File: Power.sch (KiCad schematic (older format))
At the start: 0 parts

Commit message: Put the power schematic in the wrong sub-module (PowerAdjustmentMonitor)
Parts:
- added C? (x2): C, ~, symbol C
- added F? (x4): FUSE, ~, symbol FUSE
- added L? (x2): INDUCTOR, ~, symbol INDUCTOR
- added P?: CONN_12X2, symbol CONN_12X2
- added R?: R, ~, symbol R
- added SW?: SWITCH_INV, ~, symbol SWITCH_INV
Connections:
- net labels added: +12P, +12V, +3.3V, +5V, -12P, -12V, GND
- wire segments 0 -> 36

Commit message: 3.10   Revisiting The Current/Fan Module End of Module 3, lots of cleanup/changes all over the place.
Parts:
- removed F? (x4): FUSE, ~, symbol FUSE
- added TH? (x4): THERMISTOR, ~, symbol THERMISTOR
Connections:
- net labels added: +12C
- wire segments 36 -> 33
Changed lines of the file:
@@
 $Descr A4 11693 8268
 encoding utf-8
-Sheet 4 9
+Sheet 3 9
 Title ""
 Date "10 feb 2014"
@@
 $EndComp
 $Comp
-L FUSE F?
-U 1 1 52F47ADD
-P 3800 2100
-F 0 "F?" H 3900 2150 40  0000 C CNN
-F 1 "FUSE" H 3700 2050 40  0000 C CNN
-F 2 "~" H 3800 2100 60  0000 C CNN
-F 3 "~" H 3800 2100 60  0000 C CNN
-	1    3800 2100
-	1    0    0    -1
-$EndComp
-$Comp
-L FUSE F?
-U 1 1 52F47AE3
-P 4300 2300
-F 0 "F?" H 4400 2350 40  0000 C CNN
-F 1 "FUSE" H 4200 2250 40  0000 C CNN
-F 2 "~" H 4300 2300 60  0000 C CNN
-F 3 "~" H 4300 2300 60  0000 C CNN
-	1    4300 2300
-	1    0    0    -1
-$EndComp
-$Comp
-L FUSE F?
-U 1 1 52F47AE9
-P 4800 2500
-F 0 "F?" H 4900 2550 40  0000 C CNN
-F 1 "FUSE" H 4700 2450 40  0000 C CNN
-F 2 "~" H 4800 2500 60  0000 C CNN
-F 3 "~" H 4800 2500 60  0000 C CNN
-	1    4800 2500
-	1    0    0    -1
-$EndComp
-$Comp
-L FUSE F?
-U 1 1 52F47AEF
-P 5300 2700
-F 0 "F?" H 5400 2750 40  0000 C CNN
-F 1 "FUSE" H 5200 2650 40  0000 C CNN
-F 2 "~" H 5300 2700 60  0000 C CNN
-F 3 "~" H 5300 2700 60  0000 C CNN
-	1    5300 2700
-	1    0    0    -1
-$EndComp
-$Comp
 L +12P #PWR?
 U 1 1 52F47AF5
@@
 $EndComp
 Wire Wire Line
-	1000 2200 1550 2200
-Wire Wire Line
-	1550 2200 1750 2200
+	1000 2200 1750 2200
 Wire Wire Line
 	1000 2200 1000 2300
@@
 	7800 3000 8400 3000
 Wire Wire Line
-	9000 1800 9200 1800
-Wire Wire Line
-	9200 1800 10100 1800
+	9000 1800 10100 1800
 Wire Wire Line
 	9200 1800 9200 1900
 Wire Wire Line
-	9200 2300 9200 2400
-Wire Wire Line
-	9200 2400 9200 2500
+	9200 2300 9200 2500
 Wire Wire Line
 	9200 2900 9200 3000
 Wire Wire Line
-	9000 3000 9200 3000
-Wire Wire Line
-	9200 3000 10100 3000
+	9000 3000 10100 3000
 Wire Wire Line
 	9200 2400 8800 2400
@@
 	10100 3000 10100 3100
 Connection ~ 9200 3000
+$Comp
+L THERMISTOR TH?
+U 1 1 52F82C79
+P 3800 2100
+F 0 "TH?" V 3900 2150 50  0000 C CNN
+F 1 "THERMISTOR" V 3700 2100 50  0000 C CNN
+F 2 "~" H 3800 2100 60  0000 C CNN
+F 3 "~" H 3800 2100 60  0000 C CNN
+	1    3800 2100
+	0    -1   -1   0
+$EndComp
+$Comp
+L THERMISTOR TH?
+U 1 1 52F82C86
+P 4300 2300
+F 0 "TH?" V 4400 2350 50  0000 C CNN
+F 1 "THERMISTOR" V 4200 2300 50  0000 C CNN
+F 2 "~" H 4300 2300 60  0000 C CNN
+F 3 "~" H 4300 2300 60  0000 C CNN
+	1    4300 2300
+	0    -1   -1   0
+$EndComp
+$Comp
+L THERMISTOR TH?
+U 1 1 52F82C8C
+P 4800 2500
+F 0 "TH?" V 4900 2550 50  0000 C CNN
+F 1 "THERMISTOR" V 4700 2500 50  0000 C CNN
+F 2 "~" H 4800 2500 60  0000 C CNN
+F 3 "~" H 4800 2500 60  0000 C CNN
+	1    4800 2500
+	0    -1   -1   0
+$EndComp
+$Comp
+L THERMISTOR TH?
+U 1 1 52F82C92
+P 5300 2700
+F 0 "TH?" V 5400 2750 50  0000 C CNN
+F 1 "THERMISTOR" V 5200 2700 50  0000 C CNN
+F 2 "~" H 5300 2700 60  0000 C CNN
+F 3 "~" H 5300 2700 60  0000 C CNN
+	1    5300 2700
+	0    -1   -1   0
+$EndComp
+$Comp
+L +12C #PWR?
+U 1 1 52F82C9A
+P 3300 1500
+F 0 "#PWR?" H 3300 1470 30  0001 C CNN
+F 1 "+12C" H 3300 1610 40  0000 C CNN
+F 2 "" H 3300 1500 60  0000 C CNN
+F 3 "" H 3300 1500 60  0000 C CNN
+	1    3300 1500
+	1    0    0    -1
+$EndComp
+Wire Wire Line
+	3300 1500 3300 2500
+Connection ~ 3300 2500
 $EndSCHEMATC

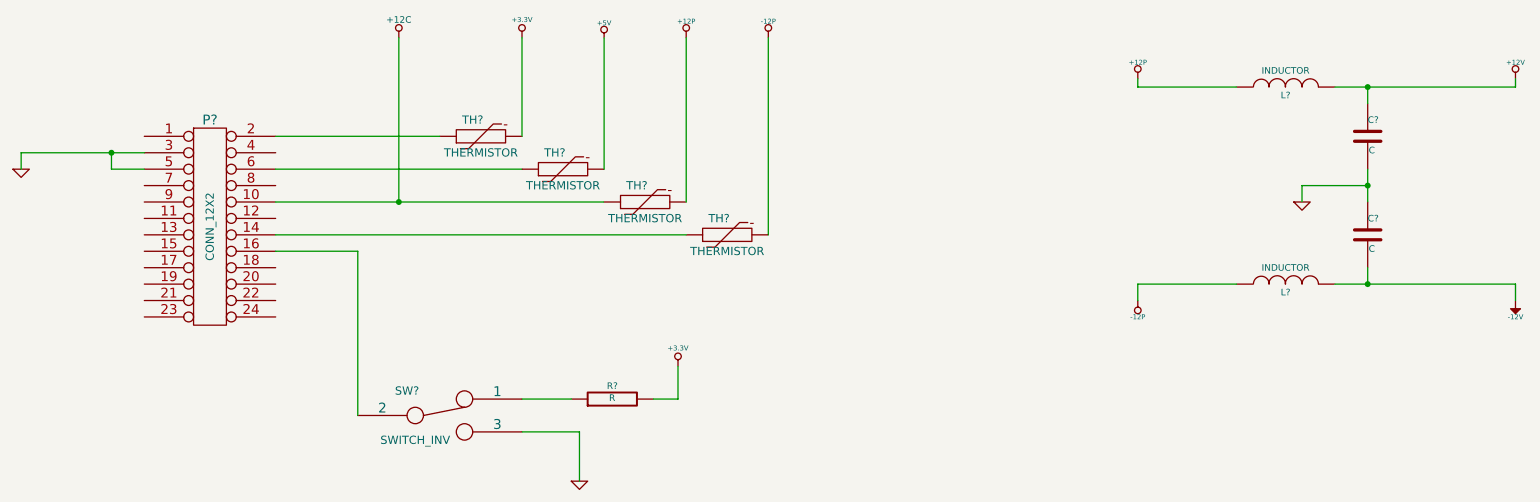
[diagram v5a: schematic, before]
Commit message: 5.3 Video 1/2 Associating and Placing the Relay Module
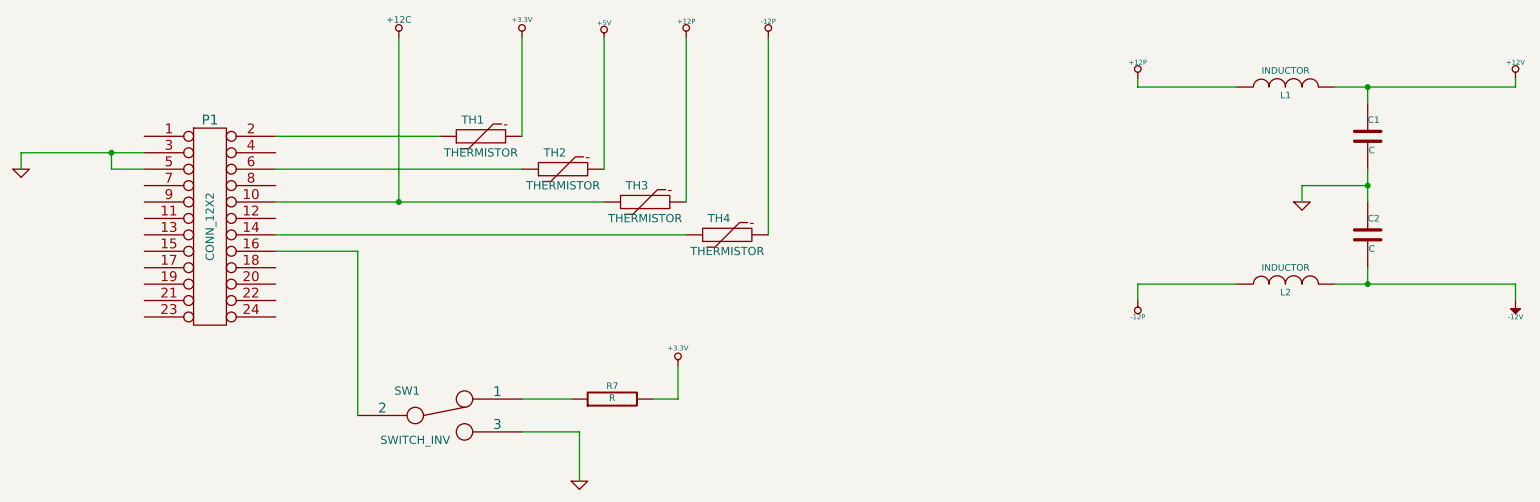
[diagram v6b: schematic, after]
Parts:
- gave numbers to parts that had none: 11
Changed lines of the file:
@@
 Sheet 3 9
 Title ""
-Date "10 feb 2014"
+Date "19 feb 2014"
 Rev ""
 Comp ""
@@
 $EndDescr
 $Comp
-L CONN_12X2 P?
+L CONN_12X2 P1
 U 1 1 52F47AD7
 P 2150 2650
-F 0 "P?" H 2150 3300 60  0000 C CNN
+F 0 "P1" H 2150 3300 60  0000 C CNN
 F 1 "CONN_12X2" V 2150 2650 50  0000 C CNN
 F 2 "" H 2150 2650 60  0000 C CNN
@@
 $EndComp
 $Comp
-L +12P #PWR?
+L +12P #PWR03
 U 1 1 52F47AF5
 P 5050 1500
-F 0 "#PWR?" H 5050 1470 30  0001 C CNN
+F 0 "#PWR03" H 5050 1470 30  0001 C CNN
 F 1 "+12P" H 5050 1600 30  0000 C CNN
 F 2 "" H 5050 1500 60  0000 C CNN
@@
 $EndComp
 $Comp
-L GND #PWR?
+L GND #PWR04
 U 1 1 52F47AFB
 P 1000 2300
-F 0 "#PWR?" H 1000 2300 30  0001 C CNN
+F 0 "#PWR04" H 1000 2300 30  0001 C CNN
 F 1 "GND" H 1000 2230 30  0001 C CNN
 F 2 "" H 1000 2300 60  0000 C CNN
@@
 Connection ~ 1550 2200
 $Comp
-L SWITCH_INV SW?
+L SWITCH_INV SW1
 U 1 1 52F47B07
 P 3550 3800
-F 0 "SW?" H 3350 3950 50  0000 C CNN
+F 0 "SW1" H 3350 3950 50  0000 C CNN
 F 1 "SWITCH_INV" H 3400 3650 50  0000 C CNN
 F 2 "~" H 3550 3800 60  0000 C CNN
@@
 	3050 2800 3050 3800
 $Comp
-L GND #PWR?
+L GND #PWR05
 U 1 1 52F47B0F
 P 4400 4200
-F 0 "#PWR?" H 4400 4200 30  0001 C CNN
+F 0 "#PWR05" H 4400 4200 30  0001 C CNN
 F 1 "GND" H 4400 4130 30  0001 C CNN
 F 2 "" H 4400 4200 60  0000 C CNN
@@
 	4400 3900 4400 4200
 $Comp
-L R R?
+L R R7
 U 1 1 52F47B17
 P 4600 3700
-F 0 "R?" V 4680 3700 40  0000 C CNN
+F 0 "R7" V 4680 3700 40  0000 C CNN
 F 1 "R" V 4607 3701 40  0000 C CNN
 F 2 "~" V 4530 3700 30  0000 C CNN
@@
 	4050 3700 4350 3700
 $Comp
-L +3.3V #PWR?
+L +3.3V #PWR06
 U 1 1 52F47B1E
 P 5000 3500
-F 0 "#PWR?" H 5000 3460 30  0001 C CNN
+F 0 "#PWR06" H 5000 3460 30  0001 C CNN
 F 1 "+3.3V" H 5000 3610 30  0000 C CNN
 F 2 "" H 5000 3500 60  0000 C CNN
@@
 	5000 3700 4850 3700
 $Comp
-L +3.3V #PWR?
+L +3.3V #PWR07
 U 1 1 52F47B26
 P 4050 1500
-F 0 "#PWR?" H 4050 1460 30  0001 C CNN
+F 0 "#PWR07" H 4050 1460 30  0001 C CNN
 F 1 "+3.3V" H 4050 1610 30  0000 C CNN
 F 2 "" H 4050 1500 60  0000 C CNN
@@
 $EndComp
 $Comp
-L +5V #PWR?
+L +5V #PWR08
 U 1 1 52F47B2C
 P 4550 1500
-F 0 "#PWR?" H 4550 1590 20  0001 C CNN
+F 0 "#PWR08" H 4550 1590 20  0001 C CNN
 F 1 "+5V" H 4550 1590 30  0000 C CNN
 F 2 "" H 4550 1500 60  0000 C CNN
@@
 $EndComp
 $Comp
-L -12P #PWR?
+L -12P #PWR09
 U 1 1 52F47B32
 P 5550 1500
-F 0 "#PWR?" H 5550 1470 30  0001 C CNN
+F 0 "#PWR09" H 5550 1470 30  0001 C CNN
 F 1 "-12P" H 5550 1600 30  0000 C CNN
 F 2 "" H 5550 1500 60  0000 C CNN
@@
 	5550 2700 5550 1500
 $Comp
-L +12P #PWR?
+L +12P #PWR010
 U 1 1 52F47B40
 P 7800 1750
-F 0 "#PWR?" H 7800 1720 30  0001 C CNN
+F 0 "#PWR010" H 7800 1720 30  0001 C CNN
 F 1 "+12P" H 7800 1850 30  0000 C CNN
 F 2 "" H 7800 1750 60  0000 C CNN
@@
 $EndComp
 $Comp
-L GND #PWR?
+L GND #PWR011
 U 1 1 52F47B46
 P 8800 2500
-F 0 "#PWR?" H 8800 2500 30  0001 C CNN
+F 0 "#PWR011" H 8800 2500 30  0001 C CNN
 F 1 "GND" H 8800 2430 30  0001 C CNN
 F 2 "" H 8800 2500 60  0000 C CNN
@@
 $EndComp
 $Comp
-L -12P #PWR?
+L -12P #PWR012
 U 1 1 52F47B4C
 P 7800 3100
-F 0 "#PWR?" H 7800 3070 30  0001 C CNN
+F 0 "#PWR012" H 7800 3070 30  0001 C CNN
 F 1 "-12P" H 7800 3200 30  0000 C CNN
 F 2 "" H 7800 3100 60  0000 C CNN
@@
 $EndComp
 $Comp
-L INDUCTOR L?
+L INDUCTOR L1
 U 1 1 52F47B52
 P 8700 1800
-F 0 "L?" V 8650 1800 40  0000 C CNN
+F 0 "L1" V 8650 1800 40  0000 C CNN
 F 1 "INDUCTOR" V 8800 1800 40  0000 C CNN
 F 2 "~" H 8700 1800 60  0000 C CNN
@@
 $EndComp
 $Comp
-L INDUCTOR L?
+L INDUCTOR L2
 U 1 1 52F47B58
 P 8700 3000
-F 0 "L?" V 8650 3000 40  0000 C CNN
+F 0 "L2" V 8650 3000 40  0000 C CNN
 F 1 "INDUCTOR" V 8800 3000 40  0000 C CNN
 F 2 "~" H 8700 3000 60  0000 C CNN
@@
 $EndComp
 $Comp
-L C C?
+L C C1
 U 1 1 52F47B5E
 P 9200 2100
-F 0 "C?" H 9200 2200 40  0000 L CNN
+F 0 "C1" H 9200 2200 40  0000 L CNN
 F 1 "C" H 9206 2015 40  0000 L CNN
 F 2 "~" H 9238 1950 30  0000 C CNN
@@
 $EndComp
 $Comp
-L C C?
+L C C2
 U 1 1 52F47B64
 P 9200 2700
-F 0 "C?" H 9200 2800 40  0000 L CNN
+F 0 "C2" H 9200 2800 40  0000 L CNN
 F 1 "C" H 9206 2615 40  0000 L CNN
 F 2 "~" H 9238 2550 30  0000 C CNN
@@
 Connection ~ 9200 2400
 $Comp
-L +12V #PWR?
+L +12V #PWR013
 U 1 1 52F47B79
 P 10100 1750
-F 0 "#PWR?" H 10100 1700 20  0001 C CNN
+F 0 "#PWR013" H 10100 1700 20  0001 C CNN
 F 1 "+12V" H 10100 1850 30  0000 C CNN
 F 2 "" H 10100 1750 60  0000 C CNN
@@
 $EndComp
 $Comp
-L -12V #PWR?
+L -12V #PWR014
 U 1 1 52F47B7F
 P 10100 3100
-F 0 "#PWR?" H 10100 3230 20  0001 C CNN
+F 0 "#PWR014" H 10100 3230 20  0001 C CNN
 F 1 "-12V" H 10100 3200 30  0000 C CNN
 F 2 "" H 10100 3100 60  0000 C CNN
@@
 Connection ~ 9200 3000
 $Comp
-L THERMISTOR TH?
+L THERMISTOR TH1
 U 1 1 52F82C79
 P 3800 2100
-F 0 "TH?" V 3900 2150 50  0000 C CNN
+F 0 "TH1" V 3900 2150 50  0000 C CNN
 F 1 "THERMISTOR" V 3700 2100 50  0000 C CNN
 F 2 "~" H 3800 2100 60  0000 C CNN
@@
 $EndComp
 $Comp
-L THERMISTOR TH?
+L THERMISTOR TH2
 U 1 1 52F82C86
 P 4300 2300
-F 0 "TH?" V 4400 2350 50  0000 C CNN
+F 0 "TH2" V 4400 2350 50  0000 C CNN
 F 1 "THERMISTOR" V 4200 2300 50  0000 C CNN
 F 2 "~" H 4300 2300 60  0000 C CNN
@@
 $EndComp
 $Comp
-L THERMISTOR TH?
+L THERMISTOR TH3
 U 1 1 52F82C8C
 P 4800 2500
-F 0 "TH?" V 4900 2550 50  0000 C CNN
+F 0 "TH3" V 4900 2550 50  0000 C CNN
 F 1 "THERMISTOR" V 4700 2500 50  0000 C CNN
 F 2 "~" H 4800 2500 60  0000 C CNN
@@
 $EndComp
 $Comp
-L THERMISTOR TH?
+L THERMISTOR TH4
 U 1 1 52F82C92
 P 5300 2700
-F 0 "TH?" V 5400 2750 50  0000 C CNN
+F 0 "TH4" V 5400 2750 50  0000 C CNN
 F 1 "THERMISTOR" V 5200 2700 50  0000 C CNN
 F 2 "~" H 5300 2700 60  0000 C CNN
@@
 $EndComp
 $Comp
-L +12C #PWR?
+L +12C #PWR015
 U 1 1 52F82C9A
 P 3300 1500
-F 0 "#PWR?" H 3300 1470 30  0001 C CNN
+F 0 "#PWR015" H 3300 1470 30  0001 C CNN
 F 1 "+12C" H 3300 1610 40  0000 C CNN
 F 2 "" H 3300 1500 60  0000 C CNN
